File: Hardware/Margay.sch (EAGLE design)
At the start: 76 parts, among them J1 SDMMC06132, J3 CONN_6SCREW_2.54, Q1 DMG3404, Q2 FDN360P, Q3 2N7002, U1 ATMEGA1284M, U10 TLV3691DPF, U11 MIC94090C6, U12 BME280, U13 MAX6070AAUT18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

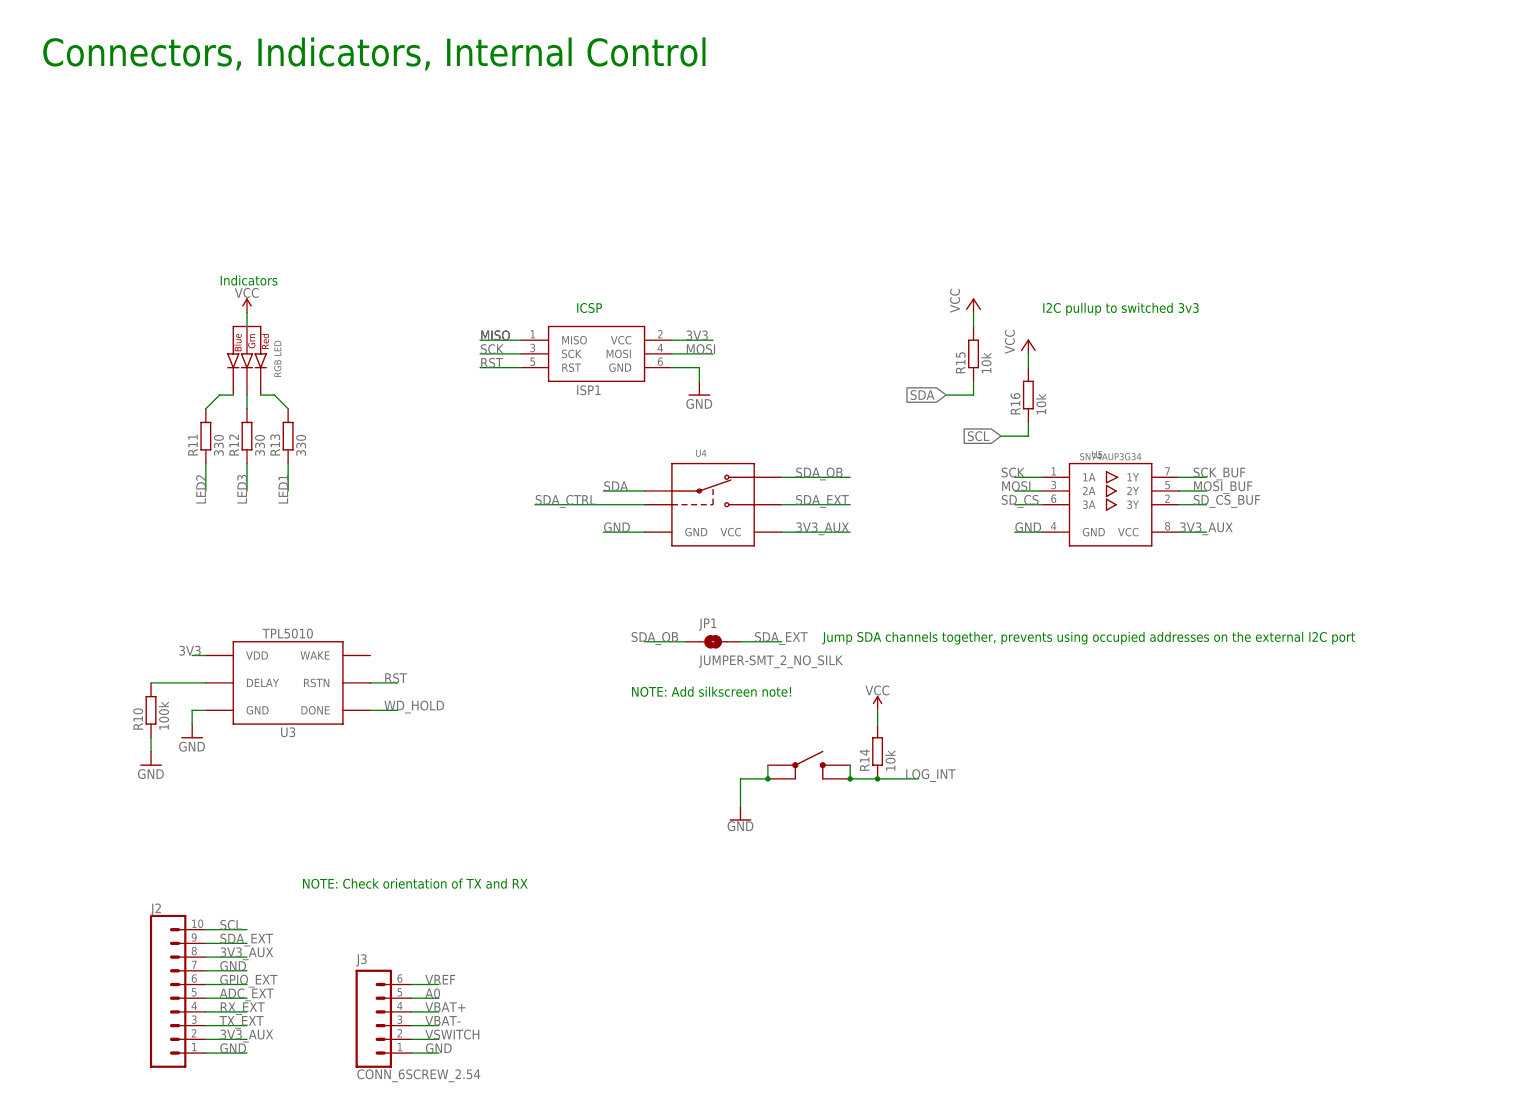
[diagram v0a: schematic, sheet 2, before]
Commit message: Cleaned up schematic and updated BoM for v2.2
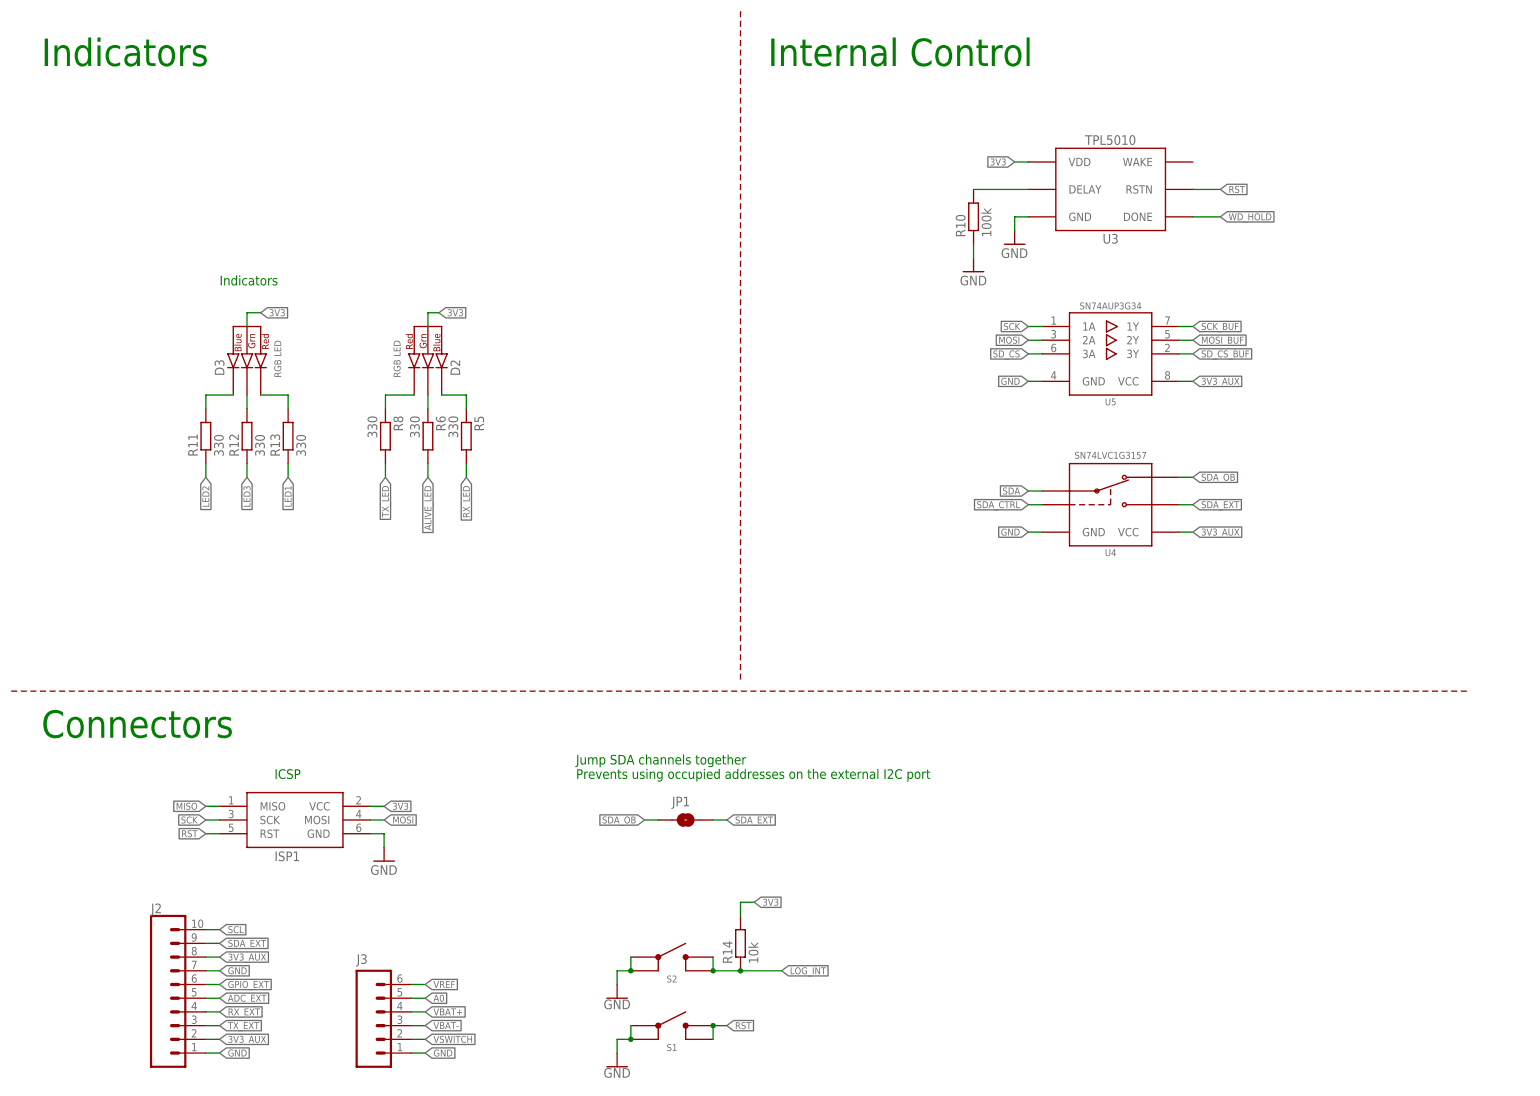
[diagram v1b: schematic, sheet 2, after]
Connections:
- net N$4 renamed RX_LED
- net N$43 renamed TX_LED
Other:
- note added: "Connectors"
- note added: "Internal Control"
- note added: "Jump SDA channels together Prevents using occupied addresses on the external I2C port"
- note added: "Jump for use with thermistor Create on board voltage divider"
- note removed: "Also ext PWM"
- note removed: "Connectors, Indicators, Internal Control"
- note removed: "Ext Int0"
- note removed: "Ext Int1"
- note removed: "Jump SDA channels together, prevents using occupied addresses on the external I2C port"
- note removed: "NOTE: Add enable line connection??"
- note removed: "NOTE: Add power switching"
- note removed: "NOTE: Add silkscreen note!"
- note removed: "NOTE: Check orientation of TX and RX"
- note removed: "NOTE: Reduce resistance?? Add capacitor in parellel"
- note removed: "USB & ISP"
- moved on the sheet: C1, C10, C11, C12, C15, C16, C17, C2, C3, C4, C5, C6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

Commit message: Updated BoM, corelated with schematic
Fixed SD card issue, fixed 0603 vs 0402 issue
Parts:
- R14, R2: DIGIKEY 311-10.0KHRCT-ND -> (none)
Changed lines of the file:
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@@
 <?xml version="1.0" encoding="utf-8"?>
 <!DOCTYPE eagle SYSTEM "eagle.dtd">
-<eagle version="9.2.1">
+<eagle version="9.4.2">
 <drawing>
 <settings>
@@
 <part name="C4" library="bschulz_passives" deviceset="C-EU" device="C0402" technology="0.1UF" value="0.1uF"/>
 <part name="GND3" library="SparkFun-PowerSymbols" deviceset="GND" device=""/>
-<part name="R2" library="bschulz_passives" deviceset="R-EU_" device="R0402" technology="10K" value="10k">
-<attribute name="DIGIKEY" value="311-10.0KHRCT-ND"/>
-</part>
+<part name="R2" library="bschulz_passives" deviceset="R-EU_" device="R0402" technology="10K" value="10k"/>
 <part name="S1" library="bschulz" deviceset="BUTTON" device="4.2X3.2"/>
 <part name="GND1" library="SparkFun-PowerSymbols" deviceset="GND" device=""/>
@@
 <part name="S2" library="bschulz" deviceset="BUTTON" device="4.2X3.2"/>
 <part name="GND17" library="SparkFun-PowerSymbols" deviceset="GND" device=""/>
-<part name="R14" library="bschulz_passives" deviceset="R-EU_" device="R0402" technology="10K" value="10k">
-<attribute name="DIGIKEY" value="311-10.0KHRCT-ND"/>
-</part>
+<part name="R14" library="bschulz_passives" deviceset="R-EU_" device="R0402" technology="10K" value="10k"/>
 <part name="D3" library="bschulz" deviceset="CLVBA-FKA" device=""/>
 <part name="R11" library="bschulz_passives" deviceset="R-EU_" device="R0402" technology="330" value="330"/>

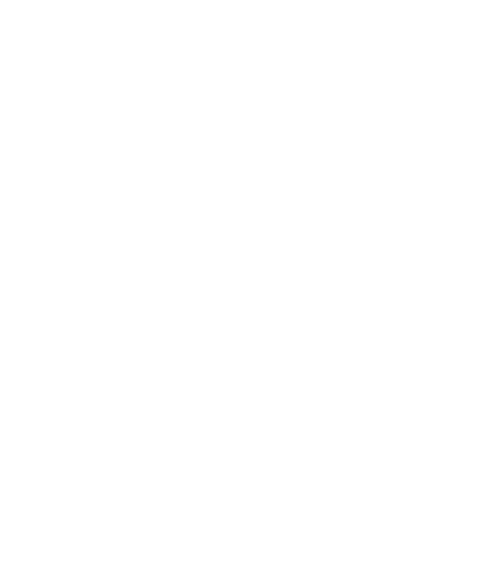
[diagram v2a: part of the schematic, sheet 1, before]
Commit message: Labeled all jumpers, including Vdiv schematic
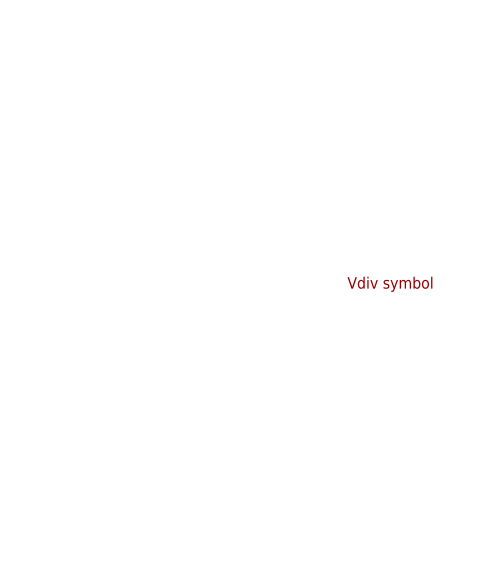
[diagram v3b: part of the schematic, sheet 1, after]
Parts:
- added U$3: VDIV_MARGAY, awickert:VDIV_MARGAY
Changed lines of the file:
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@@
 <?xml version="1.0" encoding="utf-8"?>
 <!DOCTYPE eagle SYSTEM "eagle.dtd">
-<eagle version="9.4.2">
+<eagle version="9.6.1">
 <drawing>
 <settings>
@@
 <part name="R17" library="bschulz_passives" deviceset="R-EU_" device="R0402" technology="10K" value="10k"/>
 <part name="GND18" library="supply1" library_urn="urn:adsk.eagle:library:371" deviceset="GND" device=""/>
+<part name="U$3" library="awickert" deviceset="VDIV_MARGAY" device=""/>
 </parts>
 <sheets>
@@
 <attribute name="VALUE" x="221.742" y="69.85" size="1.778" layer="96" rot="R90"/>
 </instance>
+<instance part="U$3" gate="G$1" x="264.16" y="38.1" smashed="yes"/>
 </instances>
 <busses>

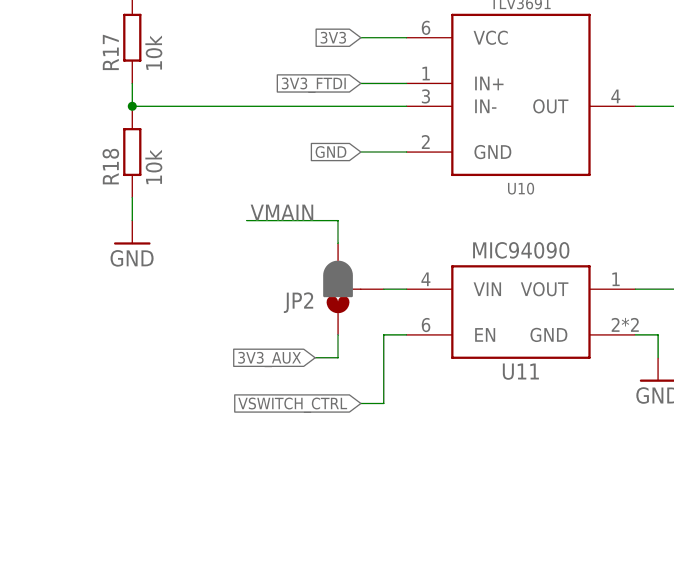
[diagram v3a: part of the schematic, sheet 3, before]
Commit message: Default Vs=Vswitch connected to 3V3_AUX via solder paste on jumper
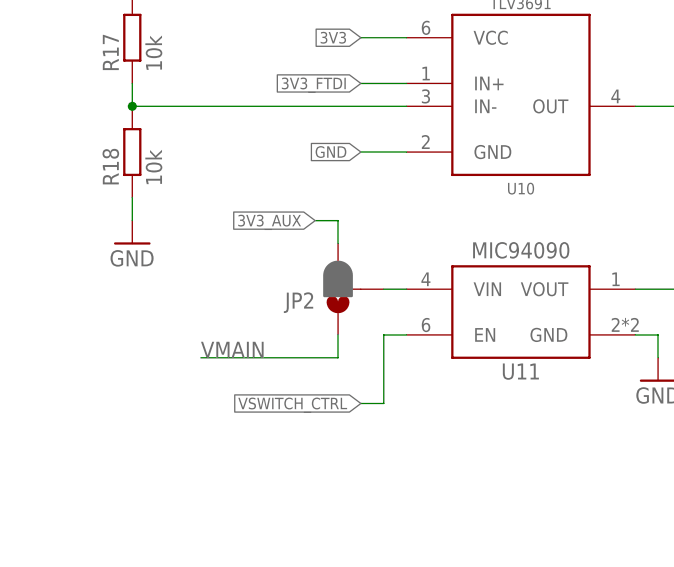
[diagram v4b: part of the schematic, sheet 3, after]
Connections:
- net 3V3_AUX: now also JP2.3; no longer JP2.1
- net VMAIN: now also JP2.1; no longer JP2.3
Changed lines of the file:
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@@
-</segment>
-<segment>
-<pinref part="JP2" gate="G$1" pin="1"/>
-<wire x1="45.72" y1="27.94" x2="45.72" y2="25.4" width="0.1524" layer="91"/>
-<wire x1="45.72" y1="25.4" x2="43.18" y2="25.4" width="0.1524" layer="91"/>
-<label x="43.18" y="25.4" size="1.27" layer="95" rot="R180" xref="yes"/>
 </segment>
 <segment>
@@
 <wire x1="190.5" y1="172.72" x2="193.04" y2="172.72" width="0.1524" layer="91"/>
 <label x="193.04" y="172.72" size="1.27" layer="95" xref="yes"/>
+</segment>
+<segment>
+<pinref part="JP2" gate="G$1" pin="3"/>
+<wire x1="45.72" y1="38.1" x2="45.72" y2="40.64" width="0.1524" layer="91"/>
+<wire x1="45.72" y1="40.64" x2="43.18" y2="40.64" width="0.1524" layer="91"/>
+<label x="43.18" y="40.64" size="1.27" layer="95" rot="R180" xref="yes"/>
 </segment>
 </net>
@@
 </segment>
 <segment>
-<pinref part="JP2" gate="G$1" pin="3"/>
-<wire x1="45.72" y1="38.1" x2="45.72" y2="40.64" width="0.1524" layer="91"/>
-<wire x1="45.72" y1="40.64" x2="35.56" y2="40.64" width="0.1524" layer="91"/>
-<label x="43.18" y="40.64" size="1.778" layer="95" rot="MR0"/>
-</segment>
-<segment>
 <pinref part="C13" gate="G$1" pin="1"/>
 <wire x1="45.72" y1="162.56" x2="50.8" y2="162.56" width="0.1524" layer="91"/>
@@
 <pinref part="U7" gate="G$1" pin="VIN"/>
 </segment>
+<segment>
+<pinref part="JP2" gate="G$1" pin="1"/>
+<wire x1="45.72" y1="27.94" x2="45.72" y2="25.4" width="0.1524" layer="91"/>
+<wire x1="45.72" y1="25.4" x2="30.48" y2="25.4" width="0.1524" layer="91"/>
+<label x="30.48" y="25.4" size="1.778" layer="95"/>
+</segment>
 </net>

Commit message: Vdiv diagram on back for jp on front
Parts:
- removed U$3: VDIV_MARGAY, awickert:VDIV_MARGAY
- added U$1: VDIV_MARGAYFULL-VDIV, awickert:VDIV_MARGAYFULL-VDIV
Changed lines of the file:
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@@
 <part name="R17" library="bschulz_passives" deviceset="R-EU_" device="R0402" technology="10K" value="10k"/>
 <part name="GND18" library="supply1" library_urn="urn:adsk.eagle:library:371" deviceset="GND" device=""/>
-<part name="U$3" library="awickert" deviceset="VDIV_MARGAY" device=""/>
+<part name="U$1" library="awickert" deviceset="VDIV_MARGAY" device="FULL-VDIV"/>
 </parts>
 <sheets>
@@
 <attribute name="VALUE" x="221.742" y="69.85" size="1.778" layer="96" rot="R90"/>
 </instance>
-<instance part="U$3" gate="G$1" x="264.16" y="38.1" smashed="yes"/>
+<instance part="U$1" gate="G$1" x="264.16" y="38.1" smashed="yes"/>
 </instances>
 <busses>

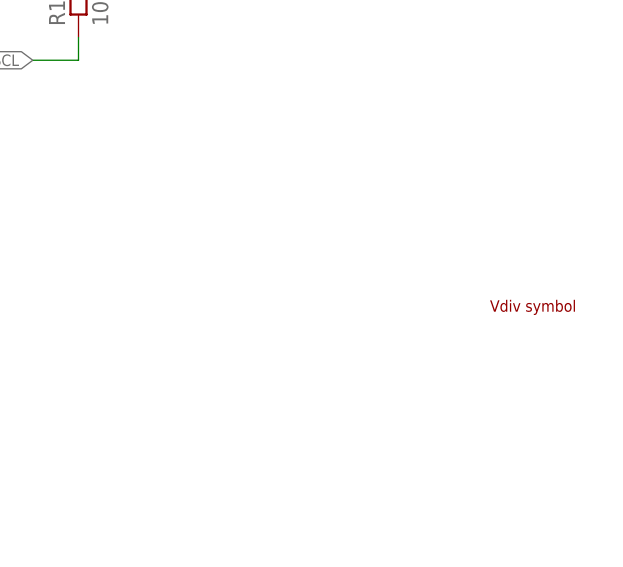
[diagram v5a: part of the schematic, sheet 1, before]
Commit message: No 4 screw holes: tight fit (ColdSilicon lbr)
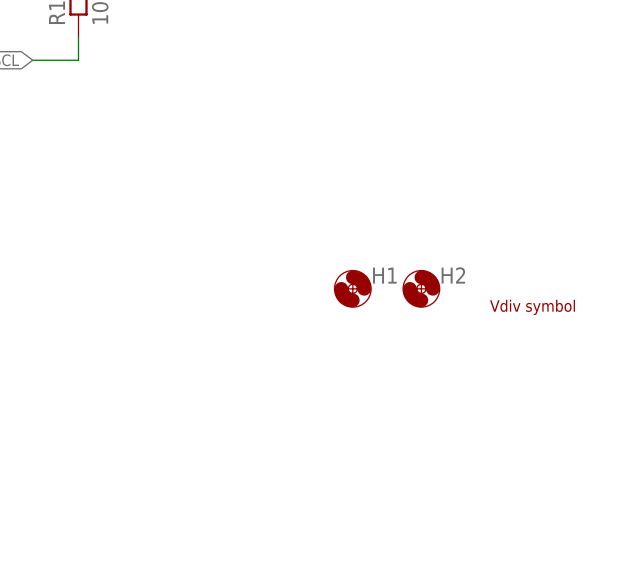
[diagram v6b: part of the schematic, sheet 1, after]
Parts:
- added H1, H2: (no value), bschulz:MOUNTING_HOLE4_NP_CLOSE
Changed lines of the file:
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@@
 <layer number="115" name="ReferenceISLANDS" color="7" fill="1" visible="yes" active="yes"/>
 <layer number="116" name="Patch_BOT" color="9" fill="4" visible="yes" active="yes"/>
+<layer number="117" name="PM_Ref" color="7" fill="1" visible="no" active="no"/>
 <layer number="118" name="Rect_Pads" color="7" fill="1" visible="yes" active="yes"/>
+<layer number="119" name="PF_Ref" color="7" fill="1" visible="no" active="no"/>
+<layer number="120" name="WFL_Ref" color="7" fill="1" visible="no" active="no"/>
 <layer number="121" name="_tsilk" color="7" fill="1" visible="yes" active="yes"/>
 <layer number="122" name="_bsilk" color="7" fill="1" visible="yes" active="yes"/>
@@
 <part name="GND18" library="supply1" library_urn="urn:adsk.eagle:library:371" deviceset="GND" device=""/>
 <part name="U$1" library="awickert" deviceset="VDIV_MARGAY" device="FULL-VDIV"/>
+<part name="H1" library="bschulz" deviceset="MOUNTING_HOLE" device="4_NP_CLOSE"/>
+<part name="H2" library="bschulz" deviceset="MOUNTING_HOLE" device="4_NP_CLOSE"/>
 </parts>
 <sheets>
@@
 </instance>
 <instance part="U$1" gate="G$1" x="264.16" y="38.1" smashed="yes"/>
+<instance part="H1" gate="G$1" x="248.92" y="40.64" smashed="yes">
+<attribute name="NAME" x="250.952" y="41.2242" size="1.778" layer="95"/>
+<attribute name="VALUE" x="250.952" y="38.1762" size="1.778" layer="96"/>
+</instance>
+<instance part="H2" gate="G$1" x="256.54" y="40.64" smashed="yes">
+<attribute name="NAME" x="258.572" y="41.2242" size="1.778" layer="95"/>
+<attribute name="VALUE" x="258.572" y="38.1762" size="1.778" layer="96"/>
+</instance>
 </instances>
 <busses>

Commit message: 100K 0402 --> 0603 for easier replacement This is on the WDT-setting resistor (R10) I changed a second resistor (R19) associated with the power system to fully convert the 0402s to 0603s and keep the number of unique items on the BoM minimal.
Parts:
- R10, R19: device bschulz_passives:R-EU_100KR0402 -> bschulz_passives:R-EU_100KR0603
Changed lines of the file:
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@@
 <part name="Q3" library="bschulz" deviceset="MOSFET-NCH" device="-2N7002PW" value="2N7002"/>
 <part name="Q2" library="bschulz" deviceset="MOSFET_PCH" device="-FDN360P" value="FDN360P"/>
-<part name="R19" library="bschulz_passives" deviceset="R-EU_" device="R0402" technology="100K" value="100k"/>
+<part name="R19" library="bschulz_passives" deviceset="R-EU_" device="R0603" technology="100K" value="100k"/>
 <part name="R21" library="bschulz_passives" deviceset="R-EU_" device="R0402" technology="10K" value="10k"/>
 <part name="GND22" library="SparkFun-PowerSymbols" library_urn="urn:adsk.eagle:library:530" deviceset="GND" device=""/>
@@
 <part name="U3" library="bschulz" deviceset="TPL5010" device="DDC"/>
 <part name="GND15" library="supply1" library_urn="urn:adsk.eagle:library:371" deviceset="GND" device=""/>
-<part name="R10" library="bschulz_passives" deviceset="R-EU_" device="R0402" technology="100K" value="100k"/>
+<part name="R10" library="bschulz_passives" deviceset="R-EU_" device="R0603" technology="100K" value="100k"/>
 <part name="GND14" library="supply1" library_urn="urn:adsk.eagle:library:371" deviceset="GND" device=""/>
 <part name="J2" library="bschulz" deviceset="CONN_10" device="2.54_SCREW"/>
@@
 </sheet>
 </sheets>
+<errors>
+</errors>
 </schematic>
 </drawing>
